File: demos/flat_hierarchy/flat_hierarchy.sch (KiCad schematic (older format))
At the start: 0 parts

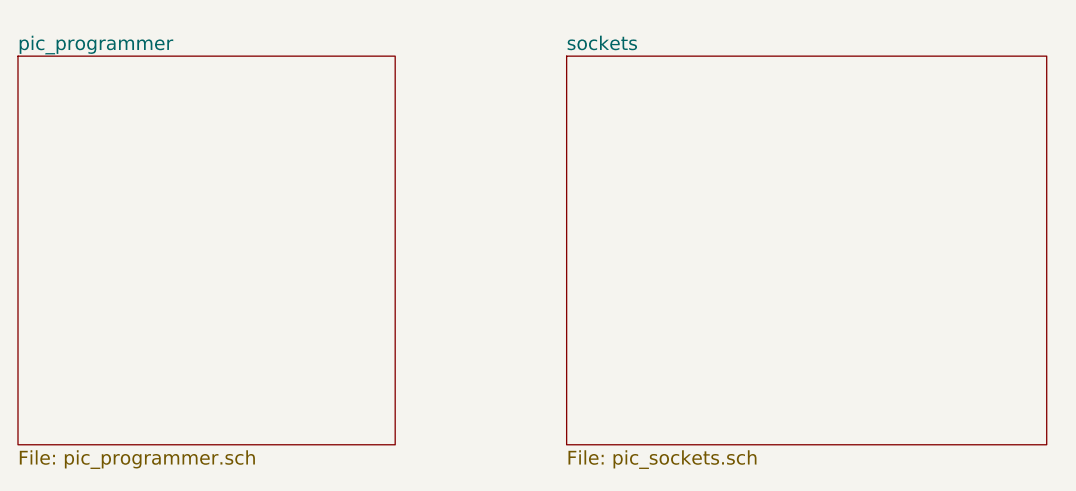
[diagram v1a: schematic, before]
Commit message: demos/ schematic tidying
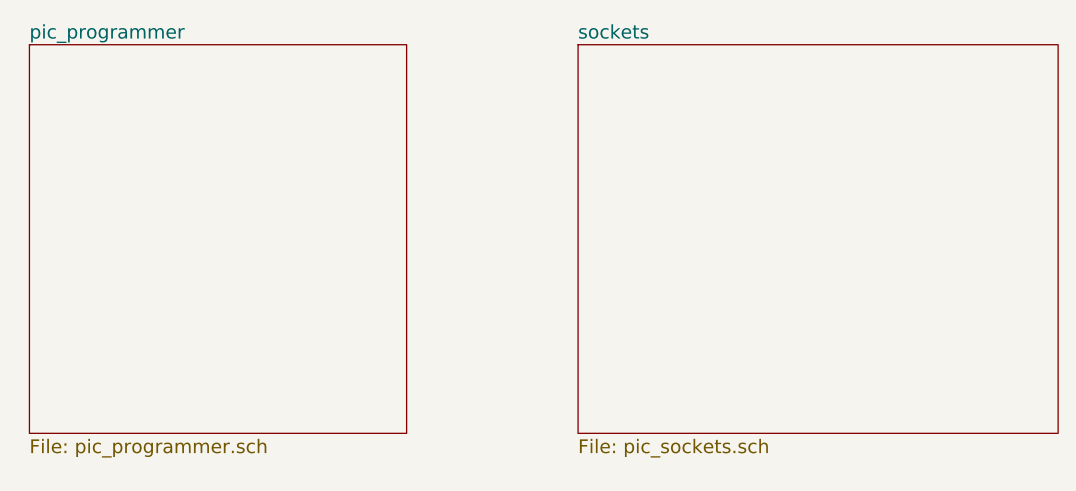
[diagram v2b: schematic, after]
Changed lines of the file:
@@
 LIBS:atmel
 LIBS:flat_hierarchy-cache
-EELAYER 24 0
+EELAYER 25 0
 EELAYER END
 $Descr A4 11693 8268
@@
 Sheet 1 3
 Title ""
-Date "15 jun 2008"
+Date "Sun 22 Mar 2015"
 Rev "1"
 Comp ""
@@
 $EndDescr
 $Sheet
-S 5550 2650 2100 1700
+S 5600 2600 2100 1700
 U 48553E7C
 F0 "sockets" 60
@@
 $EndSheet
 $Sheet
-S 3150 2650 1650 1700
+S 3200 2600 1650 1700
 U 48553E53
 F0 "pic_programmer" 60
